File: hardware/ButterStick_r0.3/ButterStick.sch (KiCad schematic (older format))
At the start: 1 part, among them J8 SYZYGY-TXR-4

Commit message: hw.r0_3: Experiment with buses
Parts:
- added U3: ECP5U25, gkl_housings_bga:caBGA_381_17x17, symbol gkl_lattice:ECP5U25-BG381
- added U6: S25FL127S, Package_SO:SOIJ-8_5.3x5.3mm_P1.27mm, symbol gkl_mem:AT25SF081
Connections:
- net labels added: +3V3, C2P_CLK_N, C2P_CLK_P, D0_N, D0_P, D1_N, D1_P, D2_N, D2_P, D3_N, D3_P, D4_N, D4_P, D5_N, D5_P, D6_N, D6_P, D7_N, D7_P, GND, P2C_CLK_N, P2C_CLK_P, QSPI_D2, QSPI_D3, S16, S17, S18, S19, S20, S21, S22, S23, S24, S25, S26, S27, SPI_CONFIG_MISO, SPI_CONFIG_MOSI, SPI_CONFIG_SCK, SPI_CONFIG_SS
- wire segments 39 -> 70
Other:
- note added: "BANK2 - 1V8"
- note added: "BANK3 - 1V8"
- moved on the sheet: J8

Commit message: hw.r0_3: cleanup and additions
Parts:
- removed J8: SYZYGY-TXR-4, gkl_conn:SYZYGY_Transcieiver, symbol gkl_misc:SYZYGY-TXR-4
- added R25: 210k, Resistor_SMD:R_0402_1005Metric, symbol Device:R
- added R26: 84k5, Resistor_SMD:R_0402_1005Metric, symbol Device:R
- added R28: 49k9, Resistor_SMD:R_0402_1005Metric, symbol Device:R
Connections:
- net GND: now also R25.2, R26.2, R28.2
- new net SYZYGY-0-STD/R_GA: R25.1
- new net SYZYGY-1-STD/R_GA: R26.1
- new net SYZYGY-2-TXR4/R_GA: R28.1
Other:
- note added: "Geographical Address: 0\nI2C Address: 0x30"
- note added: "Geographical Address: 1\nI2C Address: 0x31\n"
- note added: "Geographical Address: 2\nI2C Address: 0x32"
- moved on the sheet: U3C

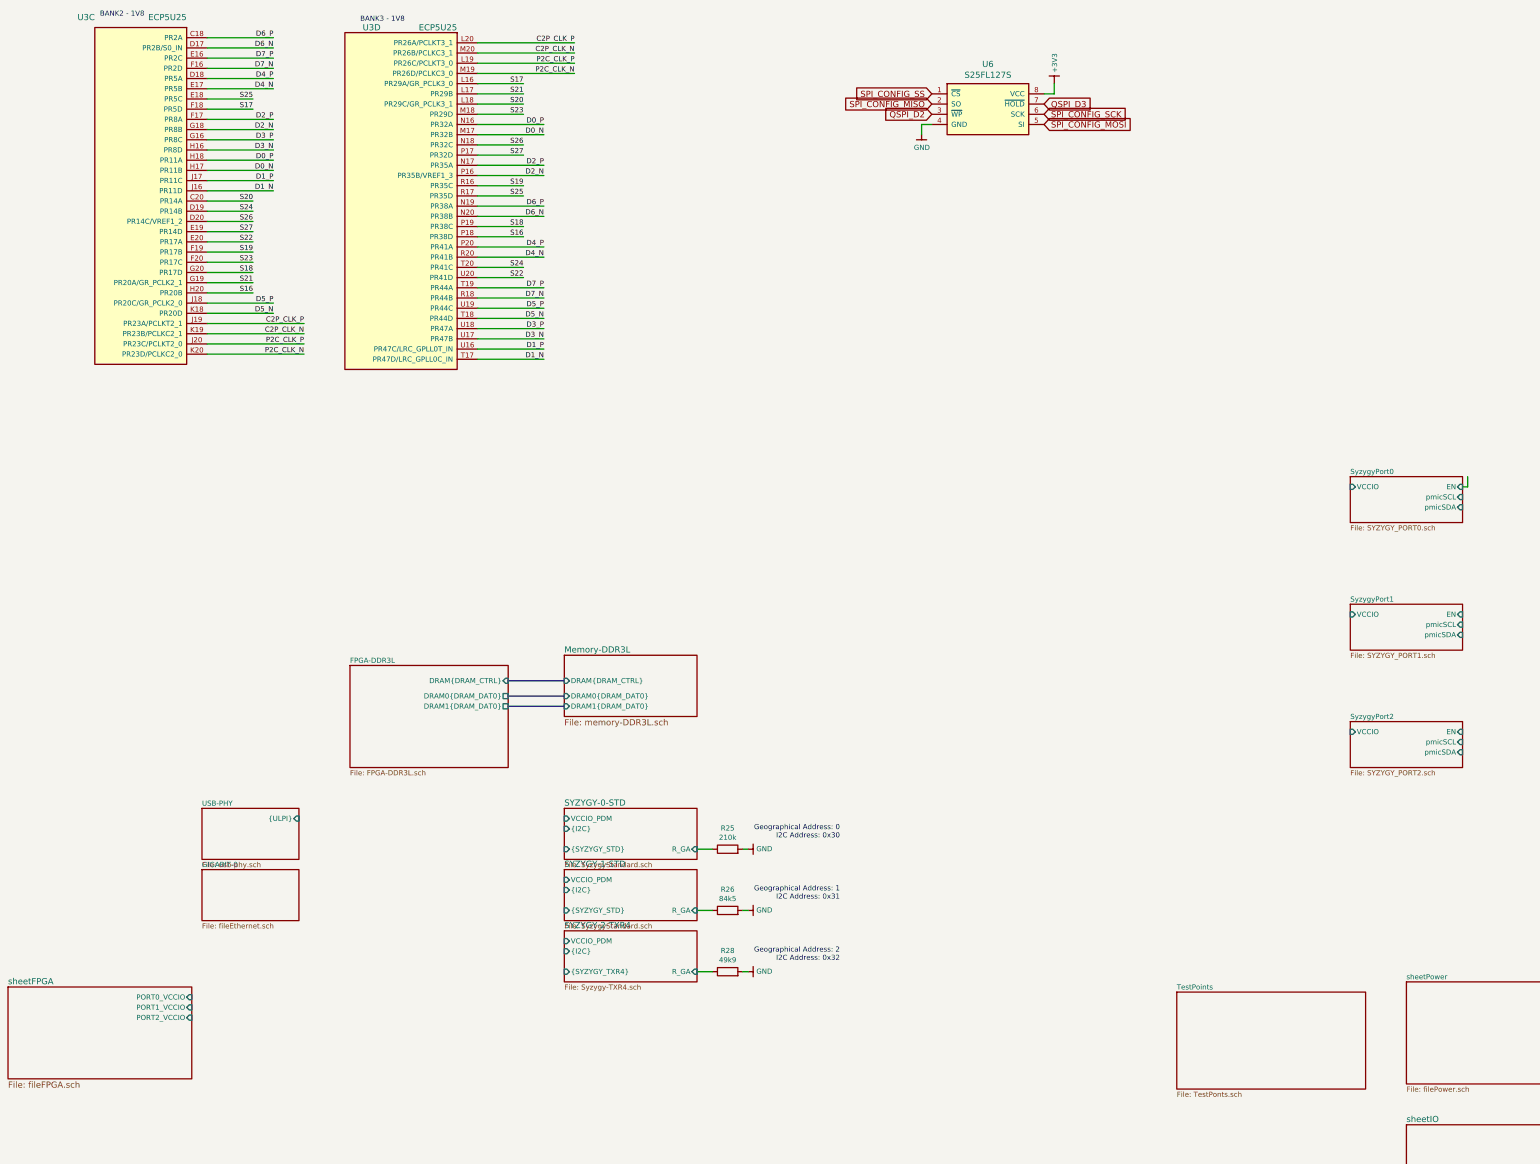
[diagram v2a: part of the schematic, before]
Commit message: hw.r0_3: Update schematics with 85F-5G symbol
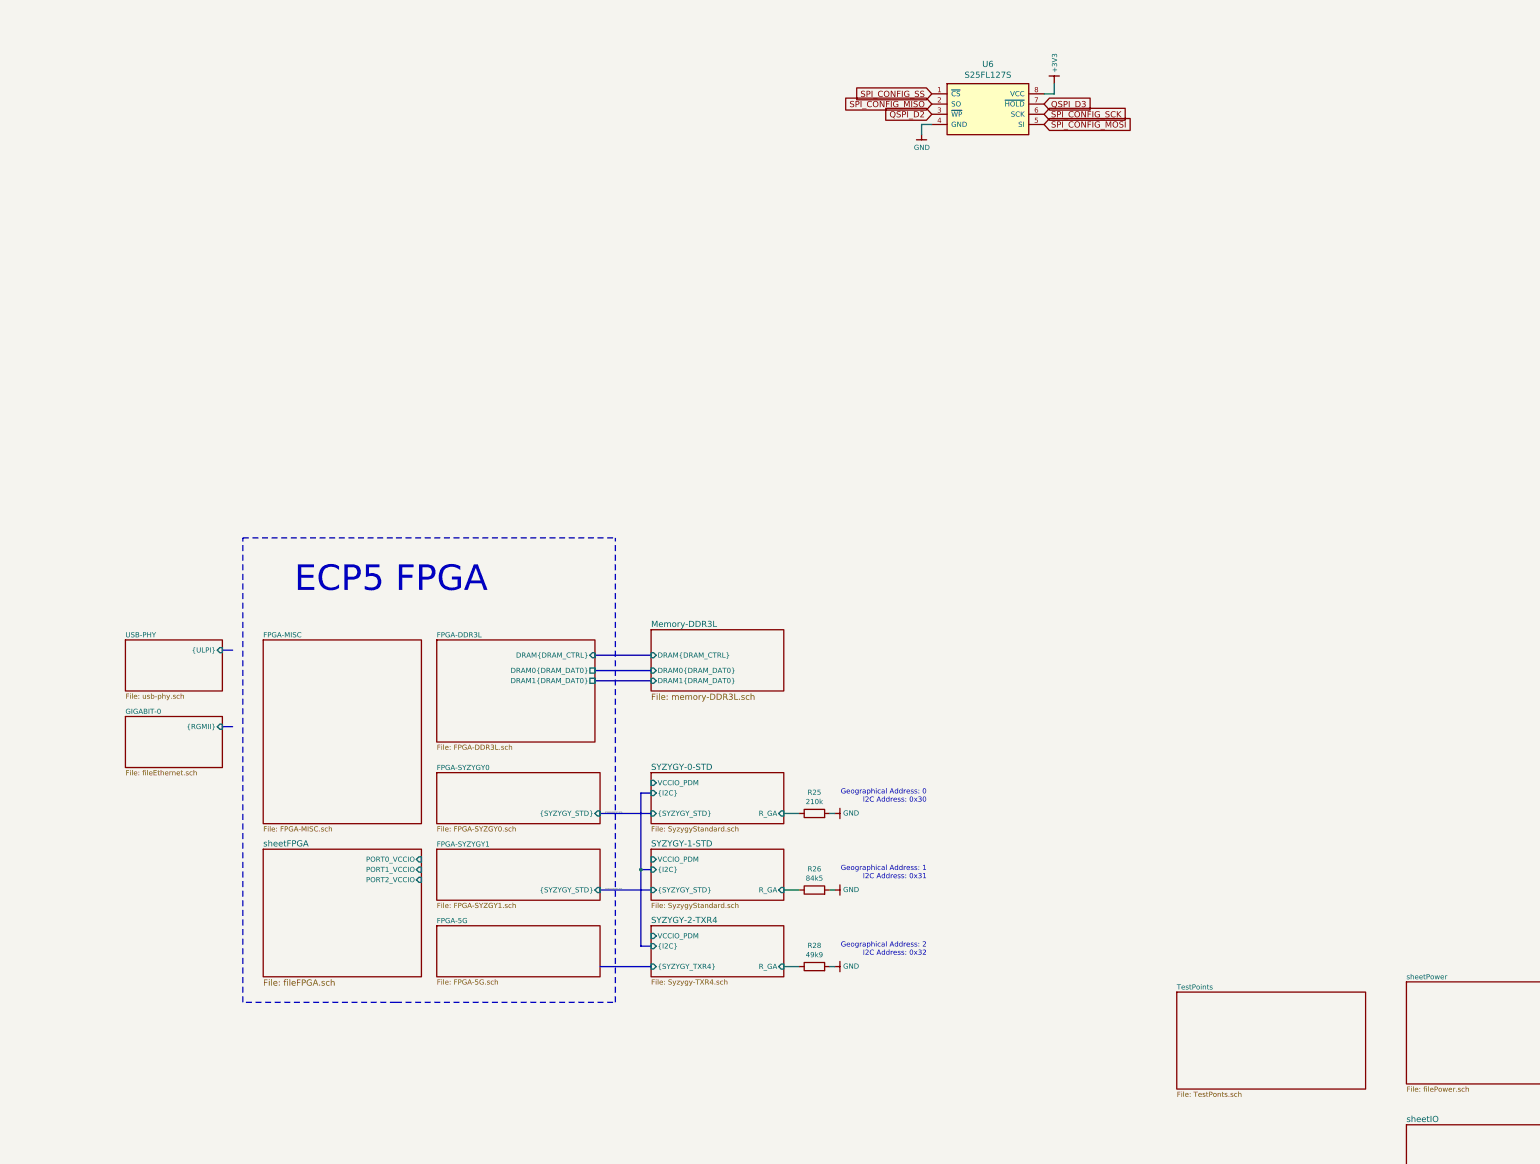
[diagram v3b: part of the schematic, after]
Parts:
- removed U3: ECP5U25, gkl_housings_bga:caBGA_381_17x17, symbol gkl_lattice:ECP5U25-BG381
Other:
- note added: "ECP5 FPGA"
- note removed: "BANK2 - 1V8"
- note removed: "BANK3 - 1V8"
- moved on the sheet: R25, R26, R28

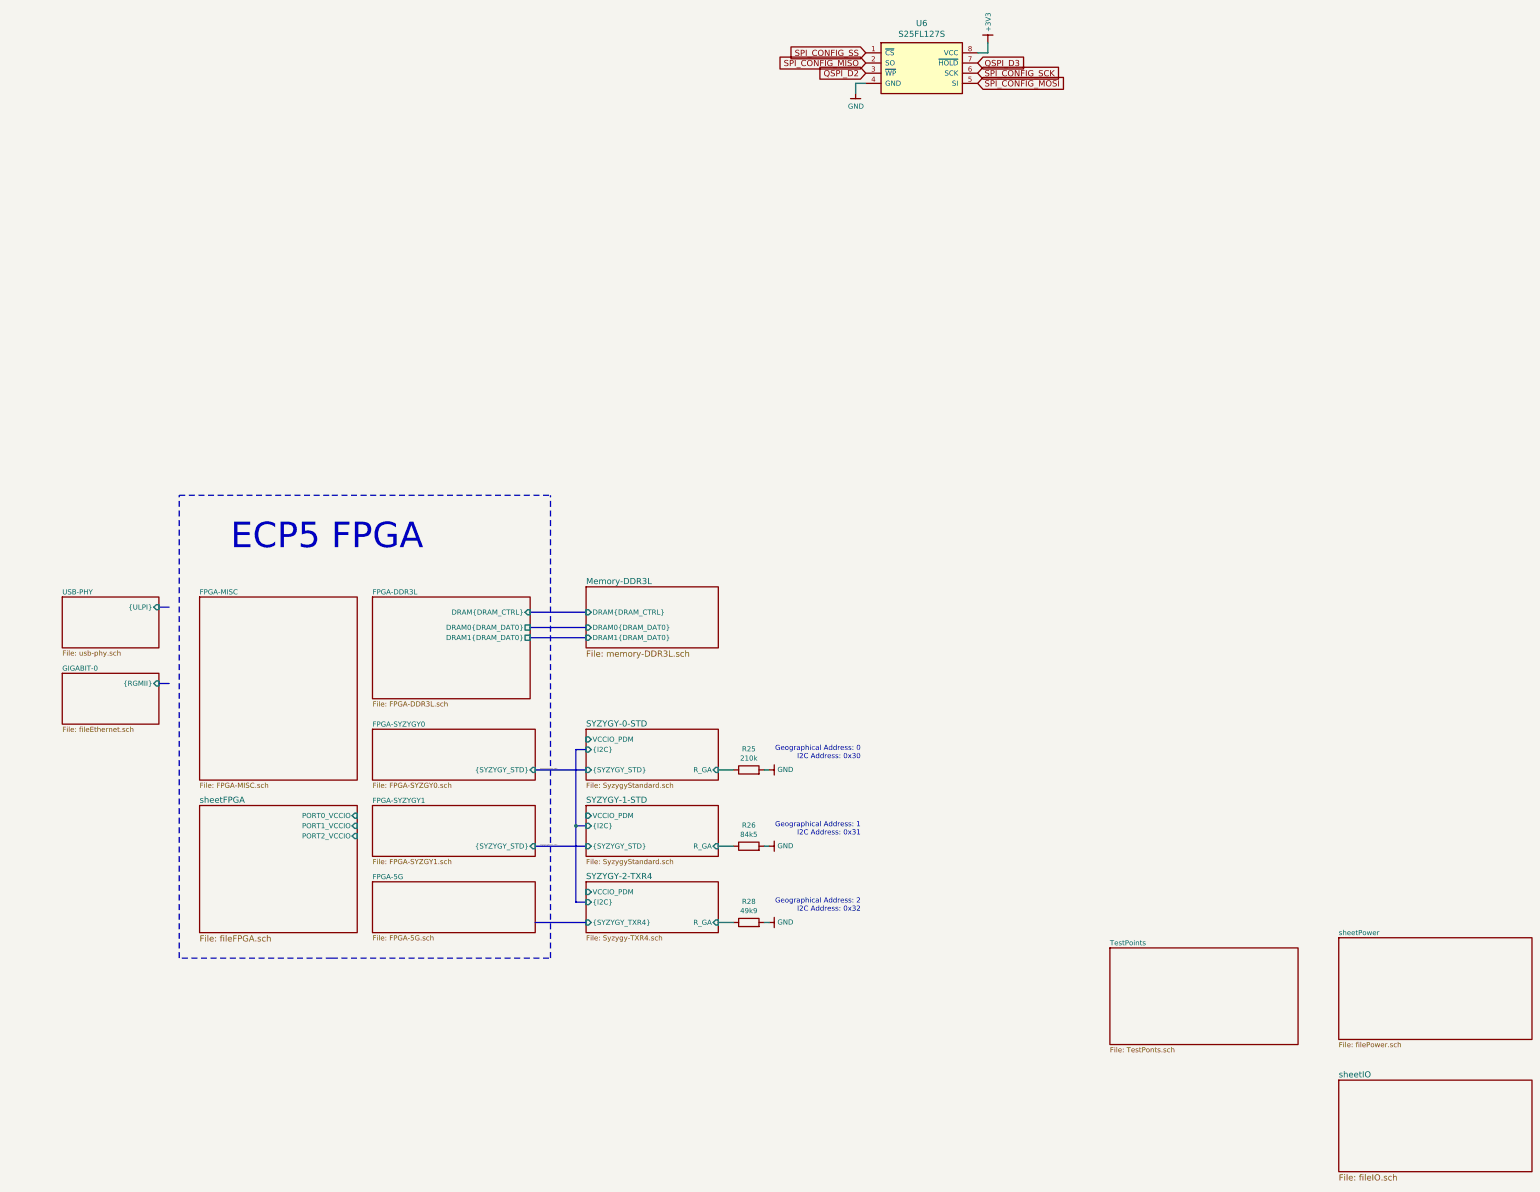
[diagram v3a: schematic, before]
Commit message: hw.r0_3: Start pin assignments for DDR3
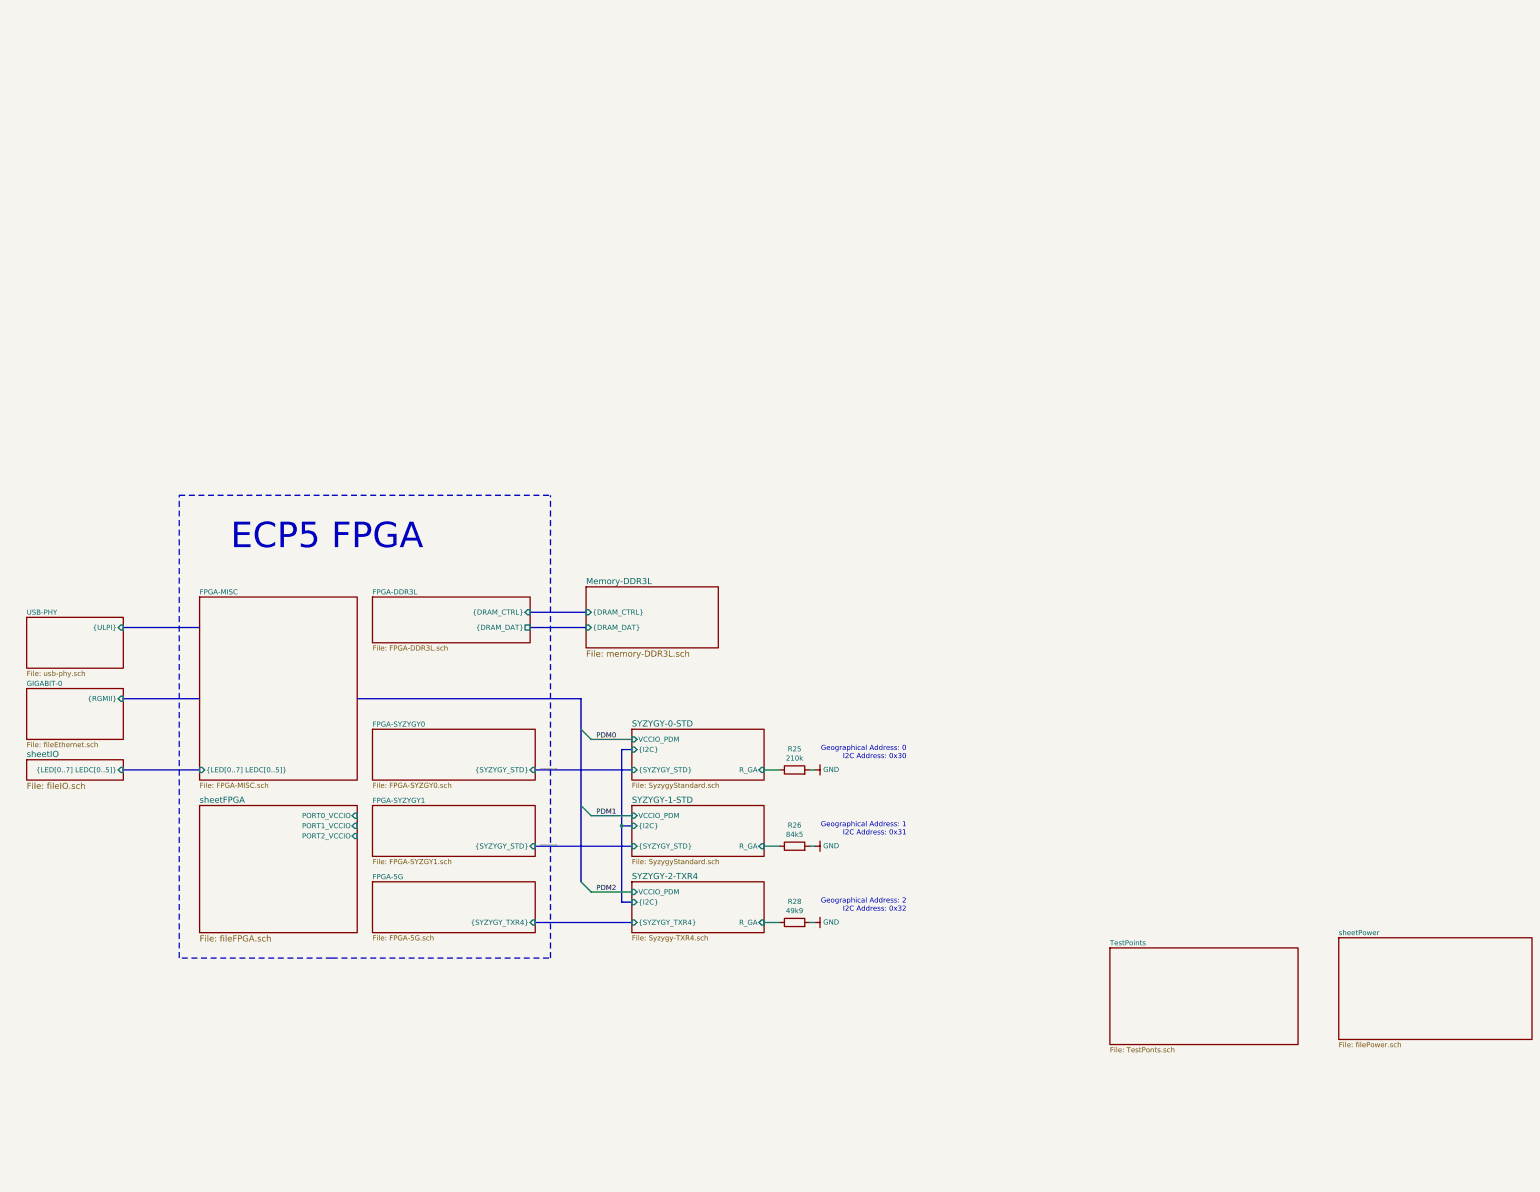
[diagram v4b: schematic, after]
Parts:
- removed U6: S25FL127S, Package_SO:SOIJ-8_5.3x5.3mm_P1.27mm, symbol gkl_mem:AT25SF081
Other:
- moved on the sheet: R25, R26, R28
